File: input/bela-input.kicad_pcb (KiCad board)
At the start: 2 copper layers, 114.3 x 31.8 mm, 67 parts, among them P1 MTA-156-4, P2 in_modular, P3 out_bela, U1 TL074, U2 TL074, U3 TL071

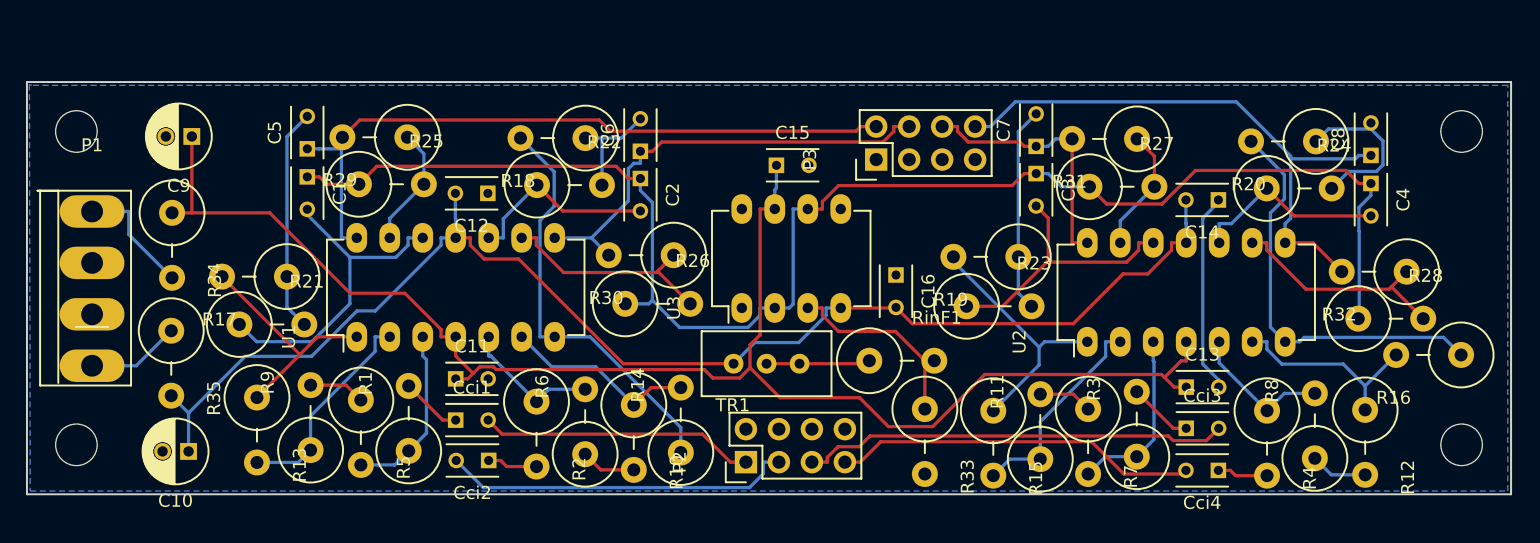
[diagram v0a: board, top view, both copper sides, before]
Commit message: moved things around, moved more to F.SilkS
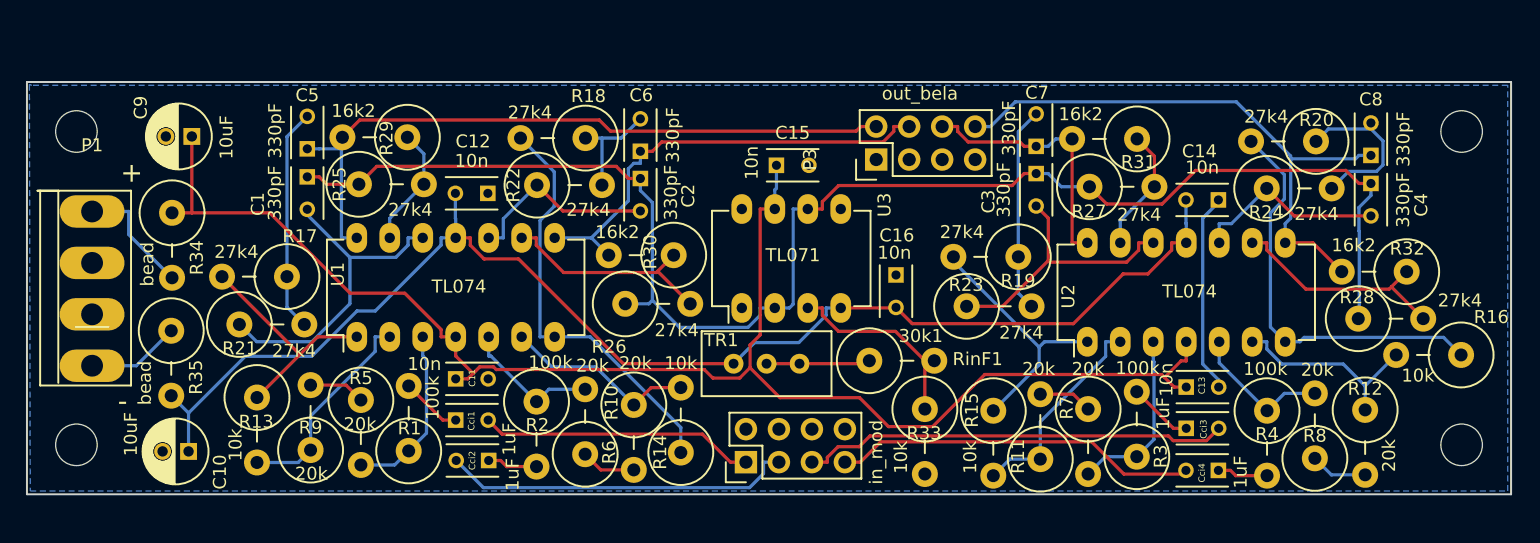
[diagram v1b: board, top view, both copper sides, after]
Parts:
- P2: value in_modular -> in_mod
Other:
- board text added: "+"
- board text added: "-"

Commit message: added more PCB documentation and moved some stuff
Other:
- board text added: "0"
- board text added: "gnd"
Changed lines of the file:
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@@
     (links 120)
     (no_connects 0)
-    (area 70.452857 68.485 196.247143 103.442548)
+    (area 76.124999 69.774999 190.575001 101.675001)
     (thickness 1.6)
-    (drawings 9)
+    (drawings 13)
     (tracks 373)
     (zones 0)
@@
   (page A4)
   (layers
-    (0 F.Cu signal hide)
-    (31 B.Cu signal hide)
+    (0 F.Cu signal)
+    (31 B.Cu signal)
     (32 B.Adhes user)
     (33 F.Adhes user)
@@
     (descr "Film Capacitor Length 4mm x Width 2.5mm, Pitch 2.5mm")
     (tags Capacitor)
-    (fp_text reference C3 (at 2.159 3.683 270) (layer F.SilkS)
-      (effects (font (size 1 1) (thickness 0.15)))
-    )
-    (fp_text value 330pF (at 1.25 2.5 270) (layer F.SilkS)
+    (fp_text reference C3 (at 2.667 3.429 270) (layer F.SilkS)
+      (effects (font (size 1 1) (thickness 0.15)))
+    )
+    (fp_text value 330pF (at 1.27 2.0955 270) (layer F.SilkS)
       (effects (font (size 1 1) (thickness 0.15)))
     )
@@
     (descr MTA-156-4)
     (tags MTA-156-4)
-    (fp_text reference P1 (at 0 -5.1) (layer F.SilkS)
+    (fp_text reference P1 (at 0 -5.1) (layer F.SilkS) hide
       (effects (font (size 1 1) (thickness 0.15)))
     )
@@
     (descr "Through hole pin header")
     (tags "pin header")
-    (fp_text reference P3 (at 0 -5.1 90) (layer F.SilkS)
-      (effects (font (size 1 1) (thickness 0.15)))
-    )
-    (fp_text value out_bela (at 5.08 3.3655 180) (layer F.SilkS)
+    (fp_text reference P3 (at 2.7305 -2.413 90) (layer F.SilkS) hide
+      (effects (font (size 1 1) (thickness 0.15)))
+    )
+    (fp_text value out_bela (at 5.08 6.1595 180) (layer F.SilkS)
       (effects (font (size 1 1) (thickness 0.15)))
     )
@@
       (net 48 "Net-(RinF1-Pad1)"))
   )
+  (gr_text 0 (at 129.2225 100.584) (layer F.SilkS)
+    (effects (font (size 1 1) (thickness 0.2)))
+  )
+  (gr_text gnd (at 139.5095 94.5515) (layer F.SilkS)
+    (effects (font (size 1 1) (thickness 0.2)))
+  )
+  (gr_text 0 (at 140.9065 70.993) (layer F.SilkS)
+    (effects (font (size 1 1) (thickness 0.25)))
+  )
+  (gr_text gnd (at 138.938 75.946 90) (layer F.SilkS)
+    (effects (font (size 1 1) (thickness 0.25)))
+  )
   (gr_text - (at 83.566 94.4245) (layer F.SilkS)

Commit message: relayout of input
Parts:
- C1, C2, C6: value 330pF -> 330p
- P2: value in_mod -> in_modular
- R1, R10, R11, R12, R13, R14, R15, R16, R17, R18, R19, R2, R20, R21, R22, R23, R24, R25, R26, R27, R28, R29, R3, R30, R31, R32, R33, R4, R5, R6, R7, R8, R9, RinF1: footprint Resistors_ThroughHole:Resistor_Vertical_RM5mm -> xnorman:Resistor_Horizontal_RM10mm-xnorman
- R34, R35: footprint Resistors_ThroughHole:Resistor_Vertical_RM5mm -> xnorman:Resistor_Vertical_RM5mm-xnor
- TR1: value TRIM -> 10k
- moved R11 20.9 mm to (153.1, 75.5), turned to 270 degrees
- moved C2 18.1 mm to (107.5, 68.6), turned to 0 degrees
- moved R27 16.4 mm to (146.6, 69.3)
- moved P3 14.5 mm to (127.8, 71.2)
- moved C3 12.5 mm to (143.9, 69.4), turned to 180 degrees
- moved C7 12.1 mm to (142.0, 72.6), turned to 270 degrees
- moved R30 11.8 mm to (124.3, 71.4)
- moved R23 11.6 mm to (149.9, 75.6), turned to 270 degrees
- moved R28 11.2 mm to (187.7, 78.9), turned to 270 degrees
- moved R15 10.9 mm to (157.4, 89.1)
- moved C5 10.7 mm to (87.1, 75.7), turned to 0 degrees
- moved C6 9.41 mm to (114.0, 74.8), turned to 0 degrees
- moved R7 9.34 mm to (153.9, 89.1)
- moved R25 9.23 mm to (102.3, 68.7), turned to 180 degrees
- moved R17 8.62 mm to (92.3, 76.3), turned to 270 degrees
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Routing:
- net GND: track 15.4 -> 194.5 mm
- net Net-(R16-Pad1): track 31.7 -> 12.1 mm
- net VSS: track 104.2 -> 116.1 mm
- net Net-(R11-Pad1): track 16.4 -> 28.0 mm
- net Net-(R3-Pad1): track 13.7 -> 25.3 mm
- net Net-(C5-Pad2): track 17.2 -> 6.08 mm
- net Net-(R14-Pad1): track 32.5 -> 22.0 mm
- net bela_ain3: track 45.2 -> 55.4 mm
- net bela_ain1: track 35.0 -> 24.8 mm
- net Net-(C4-Pad2): track 15.2 -> 24.5 mm
- net bela_ain2: track 20.2 -> 29.6 mm
- net Net-(C1-Pad2): track 25.5 -> 16.5 mm
- net Net-(R25-Pad2): track 9.36 -> 17.8 mm
- net Net-(C2-Pad2): track 15.1 -> 22.9 mm
- net Net-(R13-Pad1): track 18.1 -> 10.9 mm
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- added copper zone on F.Cu, net GND
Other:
- board size 114.3 x 31.8 mm -> 114.3 x 35.6 mm
- board text added: "modular to bela analog"
- board text removed: "mod to bela analog"
